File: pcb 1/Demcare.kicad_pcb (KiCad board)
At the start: 2 copper layers, 50 x 55.2 mm, 17 parts, among them J1 USB_B_Micro, J3 Lipo-Bat, SW2 Reset, SW3 Boot, U1 ESP32-WROOM-32, U2 CH340C, U4 TP4057, U5 MIC5504-3.3YM5

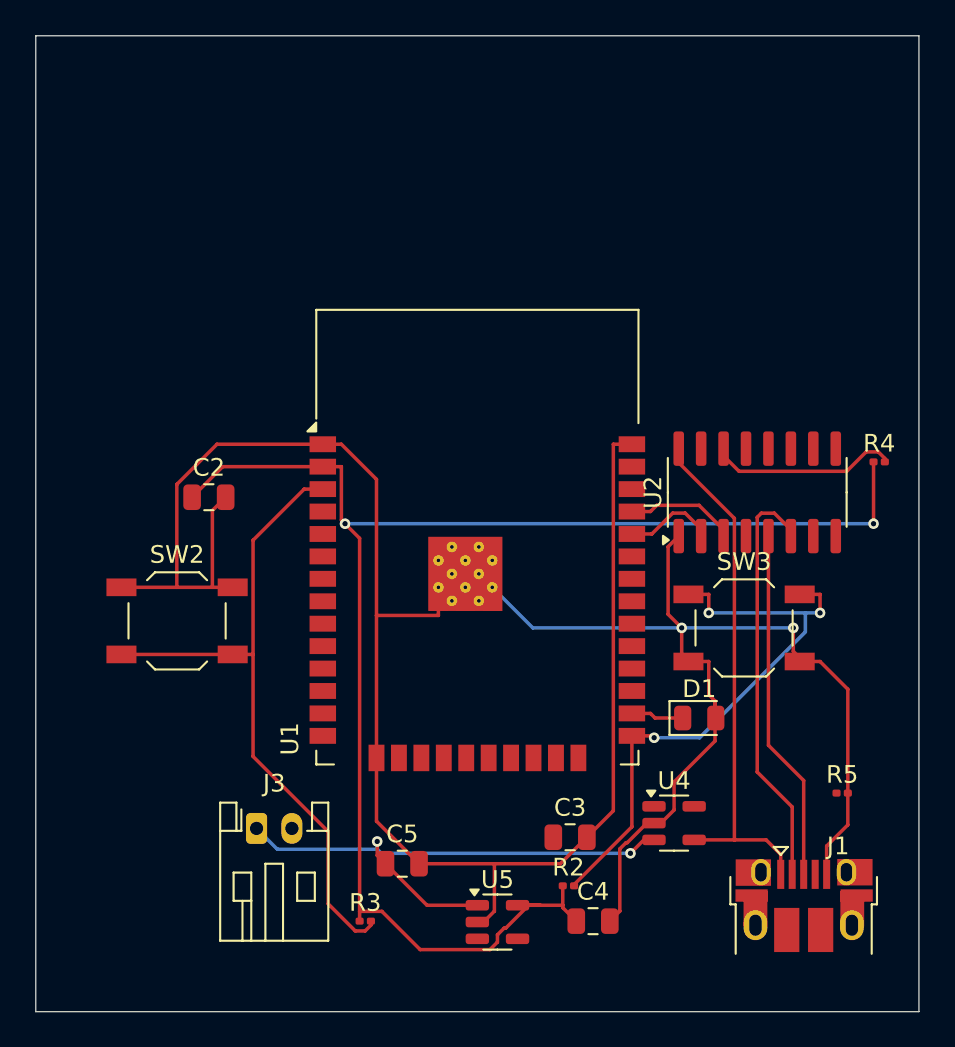
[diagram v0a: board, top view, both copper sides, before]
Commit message: rerouted the pcb
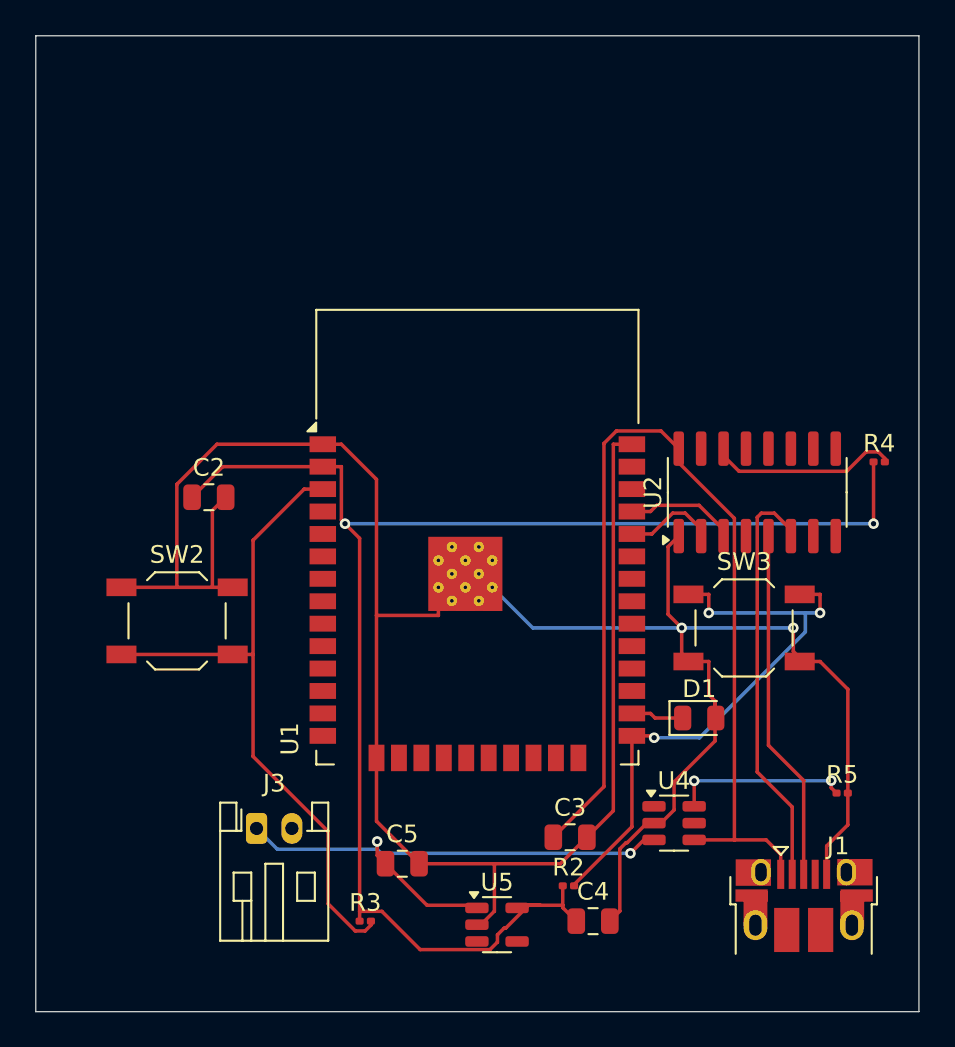
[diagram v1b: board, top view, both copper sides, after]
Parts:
- U4: footprint Package_TO_SOT_SMD:TSOT-23-5 -> Package_TO_SOT_SMD:SOT-23-6
- moved U5 0.15 mm to (129.4, 111.2)
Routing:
- net Net-(J1-VBUS): track 29.8 -> 58.2 mm
- net Net-(U4-PROG): track 0.00 -> 10.0 mm, vias 0 -> 2
- net GND: track 178.5 -> 180.8 mm
